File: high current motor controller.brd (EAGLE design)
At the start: 100 x 80 mm, 44 parts, among them Q1 IPT004N03L, Q2 IPT004N03L, Q3 IPT004N03L, Q4 IPT004N03L

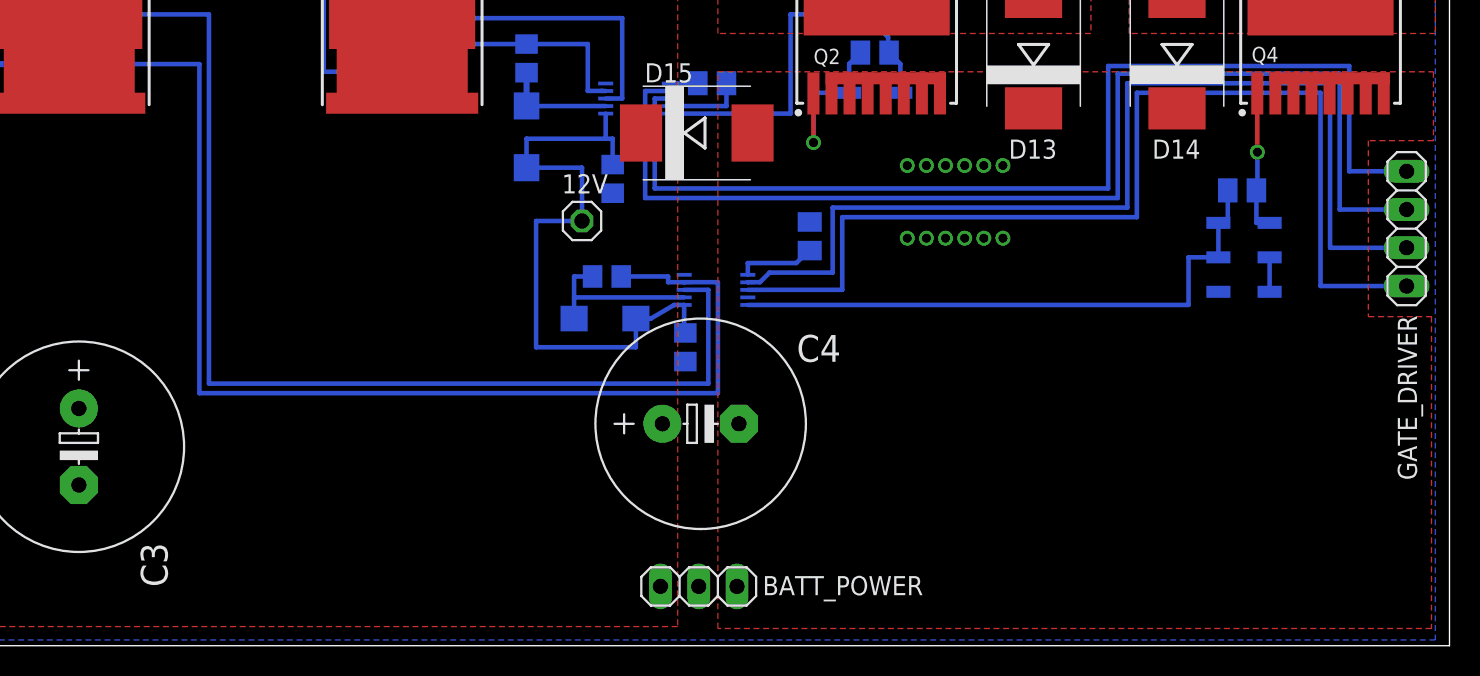
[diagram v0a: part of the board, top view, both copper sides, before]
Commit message: Add switching regulator to transform battery voltage to 12V
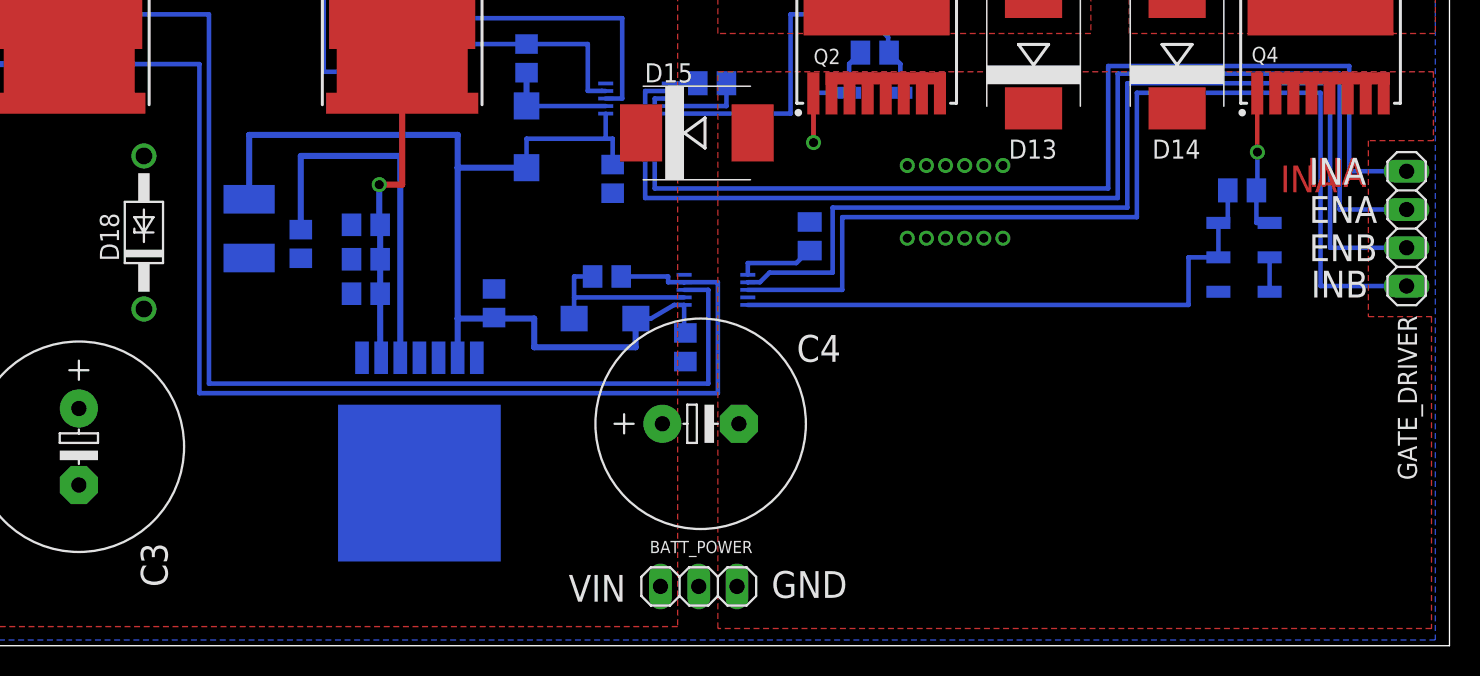
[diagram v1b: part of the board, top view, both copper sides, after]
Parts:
- removed 12V: (no value), pinhead:1X01
- added C10, C11: 15u, resistor:C0805
- added C12: 180u, resistor:C0805
- added C13: 0.01u, resistor:C0805
- added C9: 0.47u, resistor:C0805
- added D18: 1N4728, diode:DO41Z10
- added IC1: LM2676S, v-reg-3:TO263-7
- added L1: 33u, resistor:L1812
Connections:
- new net N$16: C13.1, IC1.3
- new net N$17: C13.2, D18.C, IC1.1, L1.1
- net 12V: now also C12.1, IC1.6, L1.2; no longer 12V.1
- net GND: now also C10.2, C11.2, C12.2, C9.2, D18.A, IC1.4
- net VIN: now also C10.1, C11.1, C9.1, IC1.2
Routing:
- net 12V: track 43.5 -> 69.5 mm
- net N$16: track 0.00 -> 24.9 mm
- net VIN: track 0.00 -> 19.2 mm, vias 0 -> 1
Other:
- board text added: "ENA"
- board text added: "ENB"
- board text added: "GND"
- board text added: "INA"
- board text added: "INB"
- board text added: "VIN"
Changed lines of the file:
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@@
 <layer number="107" name="Crop" color="7" fill="1" visible="no" active="yes"/>
 <layer number="116" name="Patch_BOT" color="9" fill="4" visible="no" active="yes"/>
-<layer number="121" name="_tsilk" color="7" fill="1" visible="no" active="yes"/>
+<layer number="121" name="_tsilk" color="7" fill="1" visible="yes" active="yes"/>
 <layer number="122" name="_bsilk" color="7" fill="1" visible="yes" active="yes"/>
 <layer number="151" name="HeatSink" color="7" fill="1" visible="no" active="yes"/>
@@
 <layer number="207" name="207bmp" color="8" fill="10" visible="no" active="yes"/>
 <layer number="208" name="208bmp" color="9" fill="10" visible="no" active="yes"/>
+<layer number="231" name="Eagle3D_PG1" color="7" fill="1" visible="yes" active="yes"/>
+<layer number="232" name="Eagle3D_PG2" color="7" fill="1" visible="yes" active="yes"/>
+<layer number="233" name="Eagle3D_PG3" color="7" fill="1" visible="yes" active="yes"/>
 <layer number="250" name="Descript" color="3" fill="1" visible="no" active="no"/>
 <layer number="251" name="SMDround" color="12" fill="11" visible="no" active="no"/>
@@
 <wire x1="100" y1="80" x2="0" y2="80" width="0" layer="20"/>
 <wire x1="0" y1="80" x2="0" y2="0" width="0" layer="20"/>
+<text x="90.551" y="30.607" size="1.778" layer="1">INA</text>
+<text x="90.678" y="30.48" size="1.778" layer="1">INA</text>
+<text x="90.678" y="30.48" size="1.778" layer="1">INA</text>
+<text x="90.678" y="30.48" size="1.778" layer="1">INA</text>
+<text x="90.678" y="30.48" size="1.778" layer="1">INA</text>
+<text x="88.773" y="30.099" size="1.778" layer="1">INA</text>
+<text x="90.678" y="30.607" size="1.778" layer="121">INA</text>
+<text x="90.678" y="28.067" size="1.778" layer="121">ENA</text>
+<text x="90.678" y="25.527" size="1.778" layer="121">ENB</text>
+<text x="90.805" y="23.114" size="1.778" layer="121">INB</text>
+<text x="41.529" y="2.921" size="1.778" layer="121">VIN</text>
+<text x="54.991" y="3.175" size="1.778" layer="121">GND</text>
 </plain>
 <attributes>
@@
 <attribute name="VALUE" x="53.086" y="25.273" size="0.4064" layer="28" ratio="10" rot="MR0"/>
 </element>
-<element name="12V" library="pinhead" package="1X01" value="" x="42.418" y="28.194"/>
 <element name="GATE_DRIVER" library="pinhead" package="1X04" value="" x="97.155" y="27.686" smashed="yes" rot="R270">
 <attribute name="NAME" x="96.5708" y="21.9202" size="1.27" layer="25" ratio="10" rot="R270"/>
@@
 </element>
 <element name="BATT_POWER" library="pinhead" package="1X03" value="" x="50.165" y="3.937" smashed="yes">
-<attribute name="NAME" x="54.4068" y="3.3528" size="1.27" layer="25" ratio="10"/>
+<attribute name="NAME" x="46.9138" y="6.1468" size="0.8128" layer="25" ratio="10"/>
 <attribute name="VALUE" x="46.355" y="0.762" size="1.27" layer="27"/>
 </element>
+<element name="IC1" library="v-reg-3" package="TO263-7" value="LM2676S" x="31.623" y="13.335" rot="MR180"/>
+<element name="C9" library="resistor" package="C0805" value="0.47u" x="28.067" y="23.368" rot="MR0"/>
+<element name="C10" library="resistor" package="C0805" value="15u" x="28.067" y="25.654" rot="MR0"/>
+<element name="C11" library="resistor" package="C0805" value="15u" x="28.067" y="27.94" rot="MR0"/>
+<element name="C12" library="resistor" package="C0805" value="180u" x="36.576" y="22.733" rot="MR90"/>
+<element name="C13" library="resistor" package="C0805" value="0.01u" x="23.749" y="26.67" rot="MR270"/>
+<element name="L1" library="resistor" package="L1812" value="33u" x="20.32" y="27.686" rot="MR90"/>
+<element name="D18" library="diode" package="DO41Z10" value="1N4728" x="13.335" y="27.432" rot="R90"/>
 </elements>
 <signals>
@@
 <via x="65.278" y="31.877" extent="1-16" drill="0.6"/>
 <via x="64.008" y="31.877" extent="1-16" drill="0.6"/>
-<wire x1="65.278" y1="31.877" x2="64.008" y2="31.877" width="0" layer="19" extent="1-1"/>
+<contactref element="C11" pad="2"/>
+<contactref element="IC1" pad="4"/>
+<contactref element="C10" pad="2"/>
+<contactref element="C9" pad="2"/>
+<contactref element="C12" pad="2"/>
+<contactref element="D18" pad="A"/>
+<wire x1="49.276" y1="18.862" x2="52.832" y2="14.732" width="0" layer="19" extent="16-16"/>
+<wire x1="88.44" y1="36.66" x2="81.915" y2="35.67" width="0" layer="19" extent="1-1"/>
 </signal>
 <signal name="12V">
@@
 <contactref element="C8" pad="1"/>
 <contactref element="D17" pad="A"/>
-<contactref element="12V" pad="1"/>
 <wire x1="49.276" y1="20.762" x2="49.1949" y2="20.955" width="0.3048" layer="16"/>
 <wire x1="49.1949" y1="20.955" x2="49.1949" y2="22.622" width="0.3048" layer="16"/>
@@
 <wire x1="48.532" y1="22.622" x2="46.99" y2="21.717" width="0.3048" layer="16"/>
 <wire x1="46.99" y1="21.717" x2="45.992" y2="21.717" width="0.3048" layer="16"/>
-<wire x1="42.418" y1="28.194" x2="42.418" y2="31.732" width="0.3048" layer="16"/>
-<wire x1="42.418" y1="31.732" x2="38.735" y2="31.732" width="0.3048" layer="16"/>
-<wire x1="42.418" y1="28.194" x2="39.37" y2="28.194" width="0.3048" layer="16"/>
-<wire x1="39.37" y1="28.194" x2="39.37" y2="19.812" width="0.3048" layer="16"/>
-<wire x1="39.37" y1="19.812" x2="45.992" y2="19.812" width="0.3048" layer="16"/>
-<wire x1="45.992" y1="19.812" x2="45.992" y2="21.717" width="0.3048" layer="16"/>
 <wire x1="43.9879" y1="35.322" x2="43.9879" y2="33.655" width="0.3048" layer="16"/>
 <wire x1="43.9879" y1="33.655" x2="38.735" y2="33.655" width="0.3048" layer="16"/>
@@
 <wire x1="44.45" y1="31.938" x2="44.45" y2="33.655" width="0.3048" layer="16"/>
 <wire x1="44.45" y1="33.655" x2="43.9879" y2="33.655" width="0.3048" layer="16"/>
+<contactref element="L1" pad="2"/>
+<contactref element="C12" pad="1"/>
+<contactref element="IC1" pad="6"/>
+<wire x1="20.32" y1="29.636" x2="20.32" y2="33.909" width="0.4064" layer="16"/>
+<wire x1="20.32" y1="33.909" x2="34.163" y2="33.909" width="0.4064" layer="16"/>
+<wire x1="34.163" y1="31.732" x2="34.163" y2="21.717" width="0.4064" layer="16"/>
+<wire x1="34.163" y1="21.717" x2="34.163" y2="19.115" width="0.4064" layer="16"/>
+<wire x1="34.163" y1="33.909" x2="34.163" y2="31.732" width="0.4064" layer="16"/>
+<wire x1="34.163" y1="31.732" x2="38.735" y2="31.732" width="0.4064" layer="16"/>
+<wire x1="36.576" y1="21.717" x2="34.163" y2="21.717" width="0.4064" layer="16"/>
+<wire x1="36.576" y1="21.783" x2="36.576" y2="21.717" width="0.4064" layer="16"/>
+<wire x1="36.576" y1="21.717" x2="39.243" y2="21.717" width="0.4064" layer="16"/>
+<wire x1="39.243" y1="21.717" x2="39.243" y2="19.812" width="0.4064" layer="16"/>
+<wire x1="39.243" y1="19.812" x2="45.974" y2="19.812" width="0.4064" layer="16"/>
+<wire x1="45.974" y1="19.812" x2="45.974" y2="21.717" width="0.4064" layer="16"/>
+<wire x1="45.974" y1="21.717" x2="45.992" y2="21.717" width="0.4064" layer="16"/>
 </signal>
 <signal name="N$3">
@@
 </polygon>
 <contactref element="BATT_POWER" pad="1"/>
+<contactref element="IC1" pad="2"/>
+<contactref element="C11" pad="1"/>
+<contactref element="C10" pad="1"/>
+<contactref element="C9" pad="1"/>
+<wire x1="29.083" y1="19.115" x2="29.022" y2="19.115" width="0.4064" layer="16"/>
+<wire x1="29.022" y1="19.115" x2="29.017" y2="23.368" width="0.4064" layer="16"/>
+<wire x1="29.017" y1="23.368" x2="29.017" y2="25.654" width="0.4064" layer="16"/>
+<wire x1="29.017" y1="25.654" x2="29.017" y2="27.94" width="0.4064" layer="16"/>
+<wire x1="29.017" y1="27.94" x2="28.956" y2="27.94" width="0.4064" layer="16"/>
+<wire x1="28.956" y1="27.94" x2="28.956" y2="30.607" width="0.4064" layer="16"/>
+<via x="28.956" y="30.607" extent="1-16" drill="0.6"/>
+<wire x1="28.956" y1="30.607" x2="30.48" y2="30.607" width="0.4064" layer="1"/>
+<wire x1="30.48" y1="30.607" x2="30.48" y2="36.66" width="0.4064" layer="1"/>
+</signal>
+<signal name="N$16">
+<contactref element="IC1" pad="3"/>
+<contactref element="C13" pad="1"/>
+<wire x1="30.353" y1="19.115" x2="30.353" y2="32.512" width="0.4064" layer="16"/>
+<wire x1="30.353" y1="32.512" x2="23.749" y2="32.512" width="0.4064" layer="16"/>
+<wire x1="23.749" y1="32.512" x2="23.749" y2="27.62" width="0.4064" layer="16"/>
+</signal>
+<signal name="N$17">
+<contactref element="IC1" pad="1"/>
+<contactref element="L1" pad="1"/>
+<contactref element="D18" pad="C"/>
+<contactref element="C13" pad="2"/>
+<wire x1="20.32" y1="25.736" x2="23.749" y2="25.72" width="0" layer="19" extent="16-16"/>
+<wire x1="27.813" y1="19.115" x2="23.749" y2="25.72" width="0" layer="19" extent="16-16"/>
+<wire x1="13.335" y1="22.352" x2="20.32" y2="25.736" width="0" layer="19" extent="16-16"/>
 </signal>
 </signals>
